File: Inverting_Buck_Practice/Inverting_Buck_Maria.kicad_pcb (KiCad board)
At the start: 2 copper layers, 11 parts, among them J1 Screw_Terminal_2x5.08, J2 Screw_Terminal_2x5.08, U1 MC33063AD

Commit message: Finishing another draft of Inverting Buck
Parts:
- moved J2 0.59 mm to (153.8, 149.3)
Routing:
- net GND: vias 77 -> 124
- added copper zone on F.Cu, net /V_out
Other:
- board outline added: 70.7 x 30.1 mm

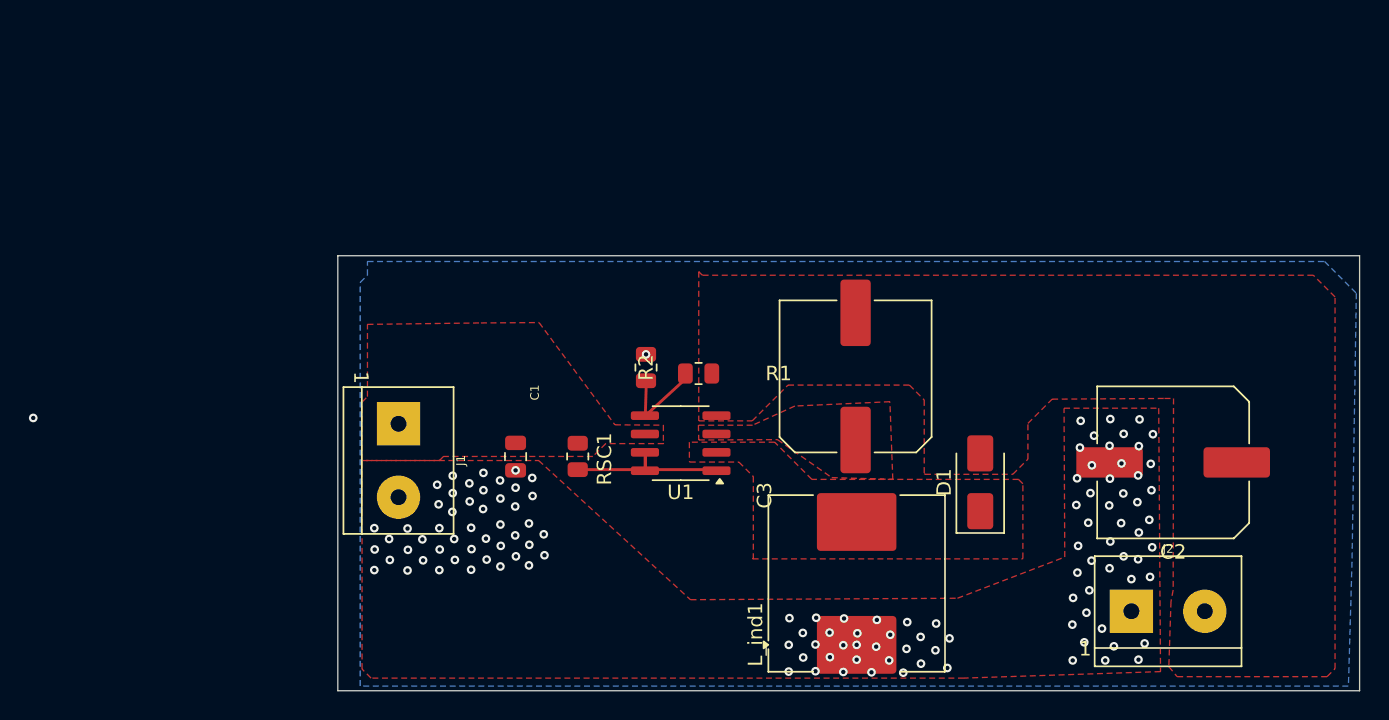
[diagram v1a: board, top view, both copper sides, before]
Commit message: Made a couple of changes, aligned the gnd and vout terminals of the screw terminal and capacitor so at to have a cleaner and wider vout/gnd copper pour, with buck having a larger Iout>Iin, so less power less internally with potetnually larger current.
Also went ahead and drew all the passive components for the IC as closer to the main body of the chip as possible, this will come into greater importance later on when working with more complicated PWM controllers, espcially with analog traces, having as close of a connection for traces conducting in the mA order succombing to greater loss the longer the distance it has to travel to communicate with the IC.

Via placemnt centralized at the capacitor (input and output, with discharge into ground requiring the greatest degree of stitching with a return path to the bottom ground layer.

Tried to make the board as tight and small as possible, the modified version is not the 'best' version. You don't hvae to make additional edits, but if you chose to you absolutely can, but regardless, where do you think the board can be improved and why? If you're not sure if there can be improvements, or feel unsure to the 'why?' part of the question, please let me know on the discord. 

I'll upload a picture of the first iteration to the README of the practie board page on github
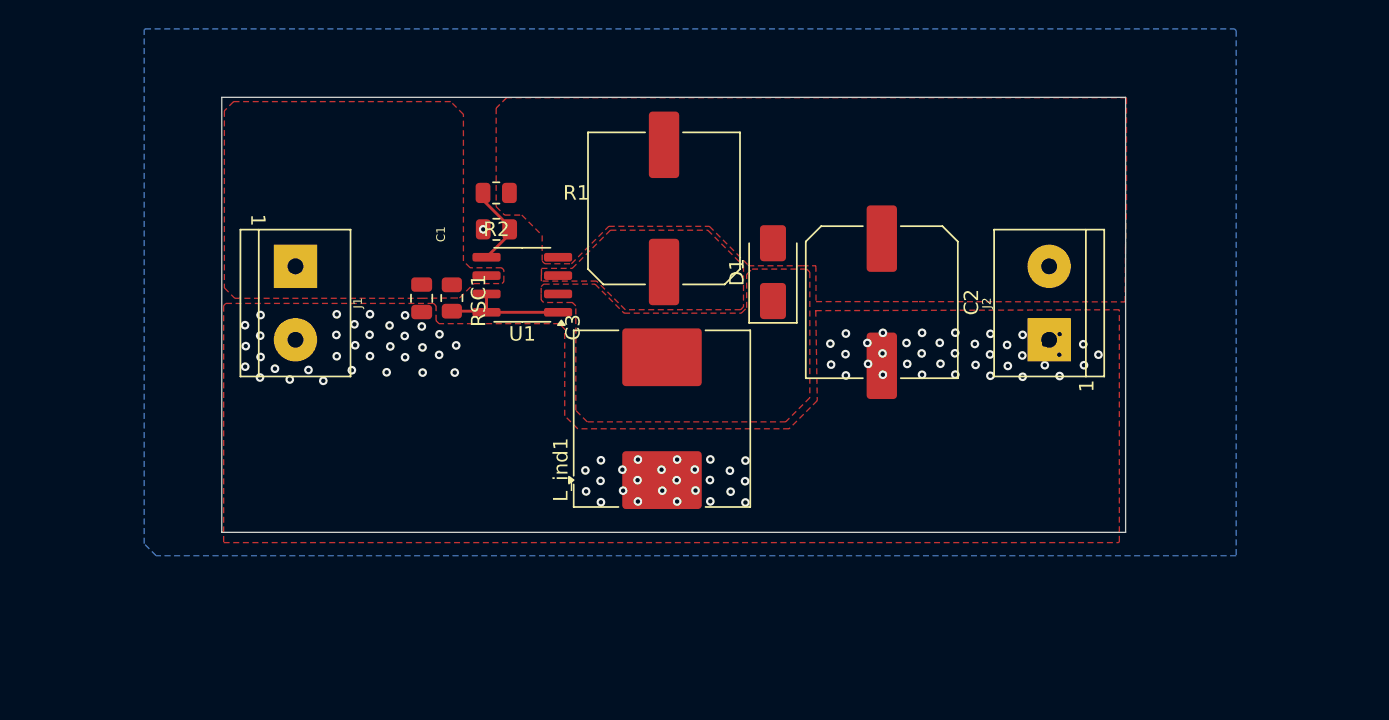
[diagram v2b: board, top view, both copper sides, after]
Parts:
- moved C2 23.0 mm to (136.5, 127.9), turned to -90 degrees
- moved D1 20.4 mm to (129.0, 125.9)
- moved J2 19.6 mm to (148.1, 130.5), turned to 90 degrees
- moved R1 18.8 mm to (109.9, 120.4)
- moved L_ind1 17.6 mm to (121.3, 136.0)
- moved C3 17.6 mm to (121.5, 121.5)
- moved U1 15.5 mm to (111.7, 126.7)
- moved R2 14.1 mm to (109.9, 122.9), turned to 180 degrees
- moved RSC1 14.0 mm to (106.8, 127.7)
- moved J1 13.0 mm to (96.0, 125.5)
- moved C1 12.7 mm to (104.7, 127.7)
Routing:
- net /V_in_after_Rsc: track 0.00 -> 8.65 mm
- net /V_volt_divider: track 0.00 -> 5.38 mm
- net GND: vias 124 -> 97
- net (no net): vias 1 -> 0
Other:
- board size 70.7 x 30.1 mm -> 62.5 x 30.1 mm
- board text added: "0.42"
